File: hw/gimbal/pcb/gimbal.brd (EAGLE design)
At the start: 68 x 42 mm, 81 parts, among them J1 JST-XH4SMT_RA, J3 JST-XH4SMT_RA, J4 MF-CON-MICROUSB-RIGHT, T12 TPPAD1-13, T3 TPPAD1-13, T8 TPPAD1-13, U1 STM32F4R_64PIN, U2 TPS62172PWSON8, U3 TPS55330PQFN16, U4 MC33926, U5 DRV8313, U6 DRV8313, U7 AS5048A

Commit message: gimbal: More manual routing.
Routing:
- net GND: track 130.4 -> 131.9 mm, vias 43 -> 44
- net +8V: track 142.3 -> 141.1 mm
- net N$3: track 9.95 -> 10.7 mm
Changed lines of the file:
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@@
 <autorouter>
 <pass name="Default">
-<param name="RoutingGrid" value="0.05mm"/>
+<param name="RoutingGrid" value="0.1mm"/>
 <param name="tpViaShape" value="round"/>
-<param name="PrefDir.1" value="*"/>
+<param name="PrefDir.1" value="\"/>
 <param name="PrefDir.2" value="0"/>
 <param name="PrefDir.3" value="0"/>
@@
 <param name="PrefDir.13" value="0"/>
 <param name="PrefDir.14" value="0"/>
-<param name="PrefDir.15" value="0"/>
-<param name="PrefDir.16" value="-"/>
+<param name="PrefDir.15" value="-"/>
+<param name="PrefDir.16" value="/"/>
 <param name="cfVia" value="8"/>
 <param name="cfNonPref" value="5"/>
@@
 <wire x1="16.6" y1="5.75" x2="16.65" y2="5.75" width="0.4064" layer="1"/>
 <via x="10.95" y="6.85" extent="1-16" drill="0.32"/>
+<wire x1="11" y1="7.85" x2="11" y2="6.85" width="0.4064" layer="1"/>
+<wire x1="11" y1="6.85" x2="10.95" y2="6.85" width="0.4064" layer="1"/>
+<via x="22.7" y="33.5" extent="1-16" drill="0.32"/>
 <wire x1="52.5" y1="25.05" x2="52.25" y2="28.3" width="0" layer="19" extent="1-1"/>
 <wire x1="20.15" y1="30.55" x2="20.15" y2="31.45" width="0" layer="19" extent="16-16"/>
-<wire x1="24.15" y1="33.65" x2="27.05" y2="34.6" width="0" layer="19" extent="1-1"/>
 <wire x1="43.95" y1="12.6" x2="43.8" y2="9.2" width="0" layer="19" extent="1-16"/>
 <wire x1="38" y1="15.25" x2="37.75" y2="18.85" width="0" layer="19" extent="1-1"/>
-<wire x1="11" y1="7.85" x2="11" y2="6.85" width="0.4064" layer="1"/>
-<wire x1="11" y1="6.85" x2="10.95" y2="6.85" width="0.4064" layer="1"/>
+<wire x1="24.15" y1="33.65" x2="22.85" y2="33.65" width="0.3048" layer="1"/>
+<wire x1="22.85" y1="33.65" x2="22.7" y2="33.5" width="0.3048" layer="1"/>
 </signal>
 <signal name="LASER_EN">
@@
 <contactref element="J2" pad="1"/>
 <wire x1="28.01" y1="3.97" x2="28.01" y2="5.81" width="0.4064" layer="1"/>
-<wire x1="28.01" y1="5.81" x2="28.8" y2="6.6" width="0.4064" layer="1"/>
-<wire x1="28.8" y1="6.6" x2="28.8" y2="10.07" width="0.4064" layer="1"/>
-<wire x1="28.8" y1="10.07" x2="27.68" y2="10.07" width="0.4064" layer="1"/>
+<wire x1="28.01" y1="5.81" x2="29.3" y2="7.1" width="0.4064" layer="1"/>
 <wire x1="27.68" y1="10.07" x2="27.68" y2="10.87" width="0.4064" layer="1"/>
 <wire x1="27.68" y1="10.87" x2="27.68" y2="11.67" width="0.4064" layer="1"/>
 <wire x1="27.68" y1="11.67" x2="27.68" y2="12.47" width="0.4064" layer="1"/>
+<wire x1="27.68" y1="10.07" x2="27.7" y2="10.07" width="0.4064" layer="1"/>
+<wire x1="27.7" y1="10.07" x2="28.8" y2="10.1" width="0.4064" layer="1"/>
+<wire x1="28.8" y1="10.1" x2="29.3" y2="10.1" width="0.4064" layer="1"/>
+<wire x1="29.3" y1="10.1" x2="29.3" y2="7.1" width="0.4064" layer="1"/>
 </signal>
 <signal name="N$5">
@@
 <wire x1="22.5" y1="27.5" x2="23.15" y2="28.15" width="0.3048" layer="1"/>
 <wire x1="23.15" y1="28.15" x2="24.15" y2="28.15" width="0.3048" layer="1"/>
-<via x="22.9" y="34.15" extent="1-16" drill="0.32"/>
-<wire x1="24.15" y1="34.15" x2="22.9" y2="34.15" width="0.3048" layer="1"/>
+<via x="22.7" y="34.35" extent="1-16" drill="0.32"/>
+<wire x1="24.15" y1="34.15" x2="23.05" y2="34.15" width="0.3048" layer="1"/>
+<wire x1="23.05" y1="34.15" x2="22.85" y2="34.35" width="0.3048" layer="1"/>
+<wire x1="22.85" y1="34.35" x2="22.7" y2="34.35" width="0.3048" layer="1"/>
 <via x="21.05" y="36.4" extent="1-16" drill="0.32"/>
 <wire x1="21.15" y1="37.65" x2="21.15" y2="36.7" width="0.3048" layer="1"/>
@@
 <wire x1="65.5" y1="25.4" x2="65.5" y2="27.15" width="1.016" layer="1"/>
 <wire x1="65.5" y1="27.15" x2="63.5" y2="27.15" width="1.016" layer="1"/>
-<wire x1="29.75" y1="10.2" x2="29.75" y2="13" width="1.016" layer="1"/>
-<wire x1="29.75" y1="10.2" x2="34.3" y2="10.2" width="1.016" layer="1"/>
+<wire x1="31.55" y1="10.2" x2="29.75" y2="13" width="1.016" layer="1"/>
+<wire x1="31.55" y1="10.2" x2="34.3" y2="10.2" width="1.016" layer="1"/>
 <wire x1="34.3" y1="10.2" x2="34.3" y2="10.3" width="1.016" layer="1"/>
 <via x="34.3" y="10.3" extent="1-16" drill="0.6"/>
@@
 <wire x1="23.38" y1="17.15" x2="23.3" y2="17.15" width="0.4064" layer="1"/>
 <wire x1="31.75" y1="32.9" x2="32.85" y2="29.3" width="0" layer="19" extent="1-1"/>
-<wire x1="31.9" y1="6.6" x2="29.75" y2="10.2" width="0" layer="19" extent="1-1"/>
+<wire x1="31.9" y1="6.6" x2="31.55" y2="10.2" width="0" layer="19" extent="1-1"/>
 </signal>
 <signal name="N$16">
@@
 <wire x1="55.45" y1="15.8" x2="57.45" y2="13.8" width="0.8128" layer="1"/>
 <wire x1="57.45" y1="13.8" x2="58.3" y2="12.9" width="0.8128" layer="1"/>
-<wire x1="58.3" y1="12.9" x2="58.3" y2="9.9" width="0.8128" layer="1"/>
-<via x="58.3" y="9.9" extent="1-16" drill="0.32"/>
-<wire x1="58.3" y1="9.9" x2="58.3" y2="6.4" width="0.8128" layer="15"/>
+<wire x1="58.3" y1="12.9" x2="58.3" y2="7.7" width="0.8128" layer="1"/>
+<via x="58.3" y="7.7" extent="1-16" drill="0.32"/>
+<wire x1="58.3" y1="7.7" x2="58.3" y2="6.4" width="0.8128" layer="15"/>
 <wire x1="58.3" y1="6.4" x2="58.3" y2="5.6" width="0.8128" layer="15"/>
 <wire x1="58.3" y1="5.6" x2="54.6" y2="5.6" width="0.8128" layer="15"/>

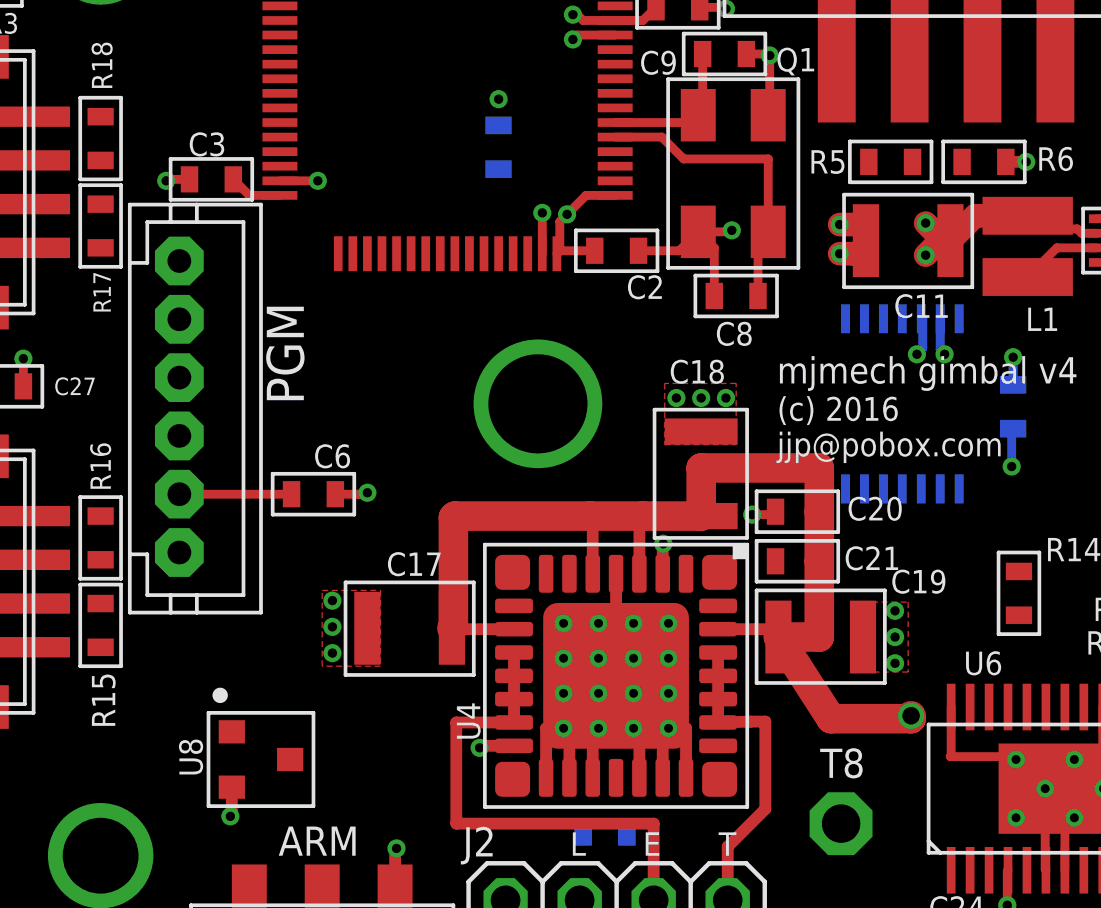
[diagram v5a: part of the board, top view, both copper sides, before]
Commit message: gimbal: Get unrouting to work.
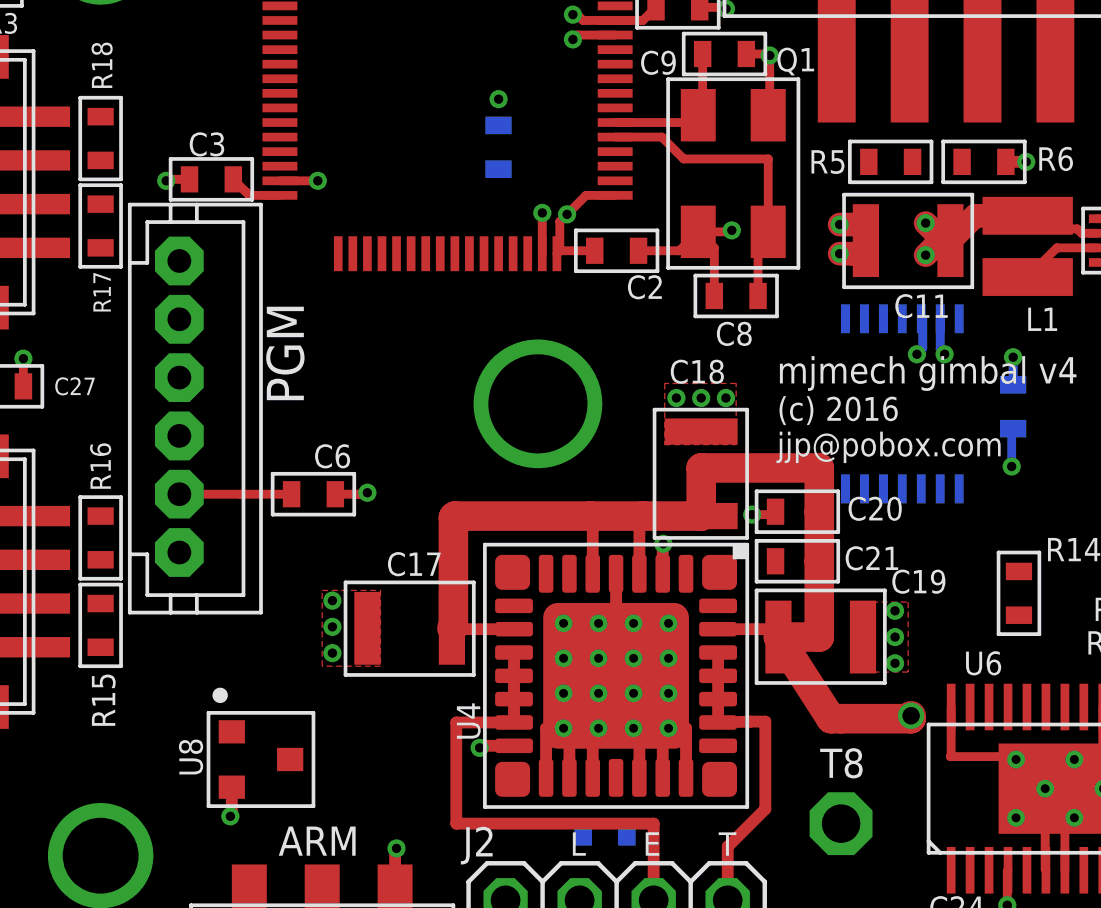
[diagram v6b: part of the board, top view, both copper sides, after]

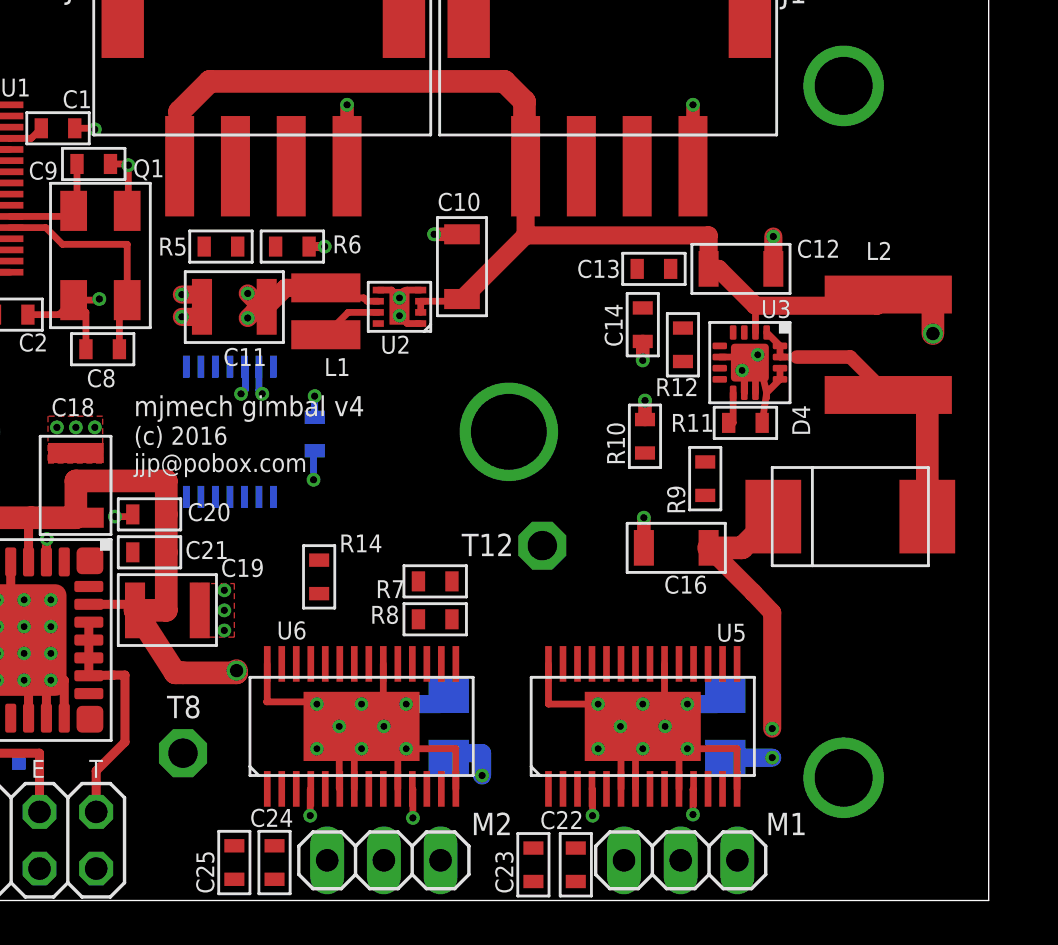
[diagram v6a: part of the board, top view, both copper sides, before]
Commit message: gimbal: Slightly tweak layout.
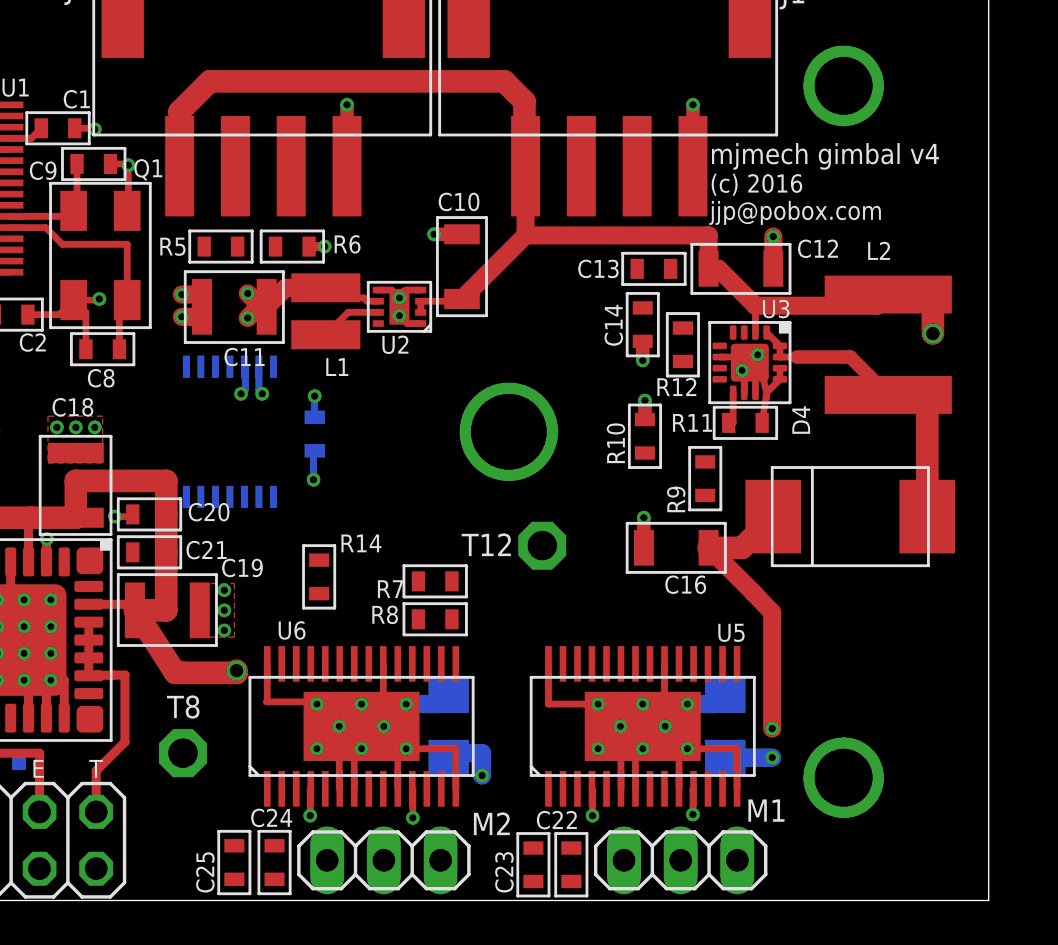
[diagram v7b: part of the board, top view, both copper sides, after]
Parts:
- moved C22 0.20 mm to (49.3, 1.60)
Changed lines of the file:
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@@
 <wire x1="68" y1="42" x2="0" y2="42" width="0" layer="20"/>
 <wire x1="0" y1="42" x2="0" y2="0" width="0" layer="20"/>
-<text x="29.7" y="19.2" size="0.8129" layer="21" ratio="10">(c) 2016
+<text x="55.5" y="30.5" size="0.8129" layer="21" ratio="10">(c) 2016
 jjp@pobox.com</text>
-<text x="29.7" y="21.7" size="0.9" layer="21" ratio="10">mjmech gimbal v4</text>
+<text x="55.5" y="33" size="0.9" layer="21" ratio="10">mjmech gimbal v4</text>
 <text x="22.6" y="5.5" size="0.8" layer="21">L</text>
 <text x="25.1" y="5.5" size="0.8" layer="21">E</text>
@@
 </element>
 <element name="M1" library="pinhead" package="1X03" value="" x="54.2" y="1.8" smashed="yes">
-<attribute name="NAME" x="58.0138" y="2.9288" size="1" layer="25" ratio="10"/>
+<attribute name="NAME" x="57.1138" y="3.5288" size="1" layer="25" ratio="10"/>
 <attribute name="VALUE" x="50.39" y="-1.375" size="1.27" layer="27"/>
 </element>
@@
 <attribute name="NAME" x="10.5" y="38.5" size="0.7" layer="25" font="vector" ratio="10" rot="R180"/>
 </element>
-<element name="C22" library="mfpassives" package="C0603" value="0.1uF" x="49.5" y="1.6" smashed="yes" rot="R90">
-<attribute name="TOLERANCE" value="N/A" x="49.5" y="1.6" size="1.778" layer="27" rot="R90" display="off"/>
-<attribute name="MFG#" value="N/A" x="49.5" y="1.6" size="1.778" layer="27" rot="R90" display="off"/>
-<attribute name="VOLTAGE" value="N/A" x="49.5" y="1.6" size="1.778" layer="27" rot="R90" display="off"/>
-<attribute name="TEMP_COF" value="N/A" x="49.5" y="1.6" size="1.778" layer="27" rot="R90" display="off"/>
-<attribute name="AMFPN" value="MF-CAP-0603-0.1uF" x="49.5" y="1.6" size="1.778" layer="27" rot="R90" display="off"/>
-<attribute name="NAME" x="47.9" y="3.2" size="0.8" layer="25" font="vector" ratio="10"/>
+<element name="C22" library="mfpassives" package="C0603" value="0.1uF" x="49.3" y="1.6" smashed="yes" rot="R90">
+<attribute name="TOLERANCE" value="N/A" x="49.3" y="1.6" size="1.778" layer="27" rot="R90" display="off"/>
+<attribute name="MFG#" value="N/A" x="49.3" y="1.6" size="1.778" layer="27" rot="R90" display="off"/>
+<attribute name="VOLTAGE" value="N/A" x="49.3" y="1.6" size="1.778" layer="27" rot="R90" display="off"/>
+<attribute name="TEMP_COF" value="N/A" x="49.3" y="1.6" size="1.778" layer="27" rot="R90" display="off"/>
+<attribute name="AMFPN" value="MF-CAP-0603-0.1uF" x="49.3" y="1.6" size="1.778" layer="27" rot="R90" display="off"/>
+<attribute name="NAME" x="47.7" y="3.2" size="0.8" layer="25" font="vector" ratio="10"/>
 </element>
 <element name="C23" library="mfpassives" package="C0603" value="0.01uF" x="47.6" y="1.6" smashed="yes" rot="R270">
